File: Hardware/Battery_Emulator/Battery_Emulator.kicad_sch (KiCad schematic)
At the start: 26 parts

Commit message: Added Cell Hierachy
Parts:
- removed C? (x5): C, Capacitor_SMD:C_0805_2012Metric, symbol Device:C
- removed JP? (x2): Jumper_3_Bridged12, symbol Jumper:Jumper_3_Bridged12
- removed PS?: MEE1S1209SC, Converter_DCDC:Converter_DCDC_Murata_MEE1SxxxxSC_THT, symbol Converter_DCDC:MEE1S1209SC
- removed Q?: IRF7343PBF, Package_SO:SOIC-8_3.9x4.9mm_P1.27mm, symbol Transistor_FET:IRF7343PBF
- removed R? (x4): R, Resistor_SMD:R_0805_2012Metric, symbol Device:R
- removed RV? (x2): R_POT, symbol Device:R_POT
- removed U? (x2): 74AHC2G125DP,125, Package_SO:TSSOP-8_3x3mm_P0.65mm, symbol Regulator_Linear:L7805
- removed U?: 74AHC2G125DP,125, Package_SO:TSSOP-8_3x3mm_P0.65mm, symbol Regulator_Linear:LM317L_TO92
- removed U? (x3): 74AHC2G125DP,125, Package_SO:TSSOP-8_3x3mm_P0.65mm, symbol Amplifier_Operational:TL072
- removed U? (x2): 74AHC2G125DP,125, Package_SO:TSSOP-8_3x3mm_P0.65mm, symbol 74xGxx:74AUC2G125
- removed U?: 74AHC2G125DP,125, Package_SO:TSSOP-8_3x3mm_P0.65mm, symbol PR7 Custom:ISO1640BDR
- removed U?: 74AHC2G125DP,125, Package_SO:TSSOP-8_3x3mm_P0.65mm, symbol PR7 Custom:MCP4651T-103E_ST
- added J1: Screw_Terminal_01x02, symbol Connector:Screw_Terminal_01x02
- added U3: 74AHC2G125DP,125, Package_SO:TSSOP-8_3x3mm_P0.65mm, symbol PR7 Custom:74AHC2G125DP,125
- added U5: LM7805_TO220, Package_TO_SOT_THT:TO-220-3_Vertical, symbol Regulator_Linear:LM7805_TO220
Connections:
- net GND: now also J1.2 (Pin_2), U5.2 (GND)
- net +12V: now reaches C?.1
- net +12V: now also J1.1 (Pin_1), U5.1 (VI)
- new net +5V: U5.3 (VO)
- new net SDA_cell_1-7: U3.6
- new net SDA_cell_8-14: U3.3
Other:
- moved on the sheet: C?

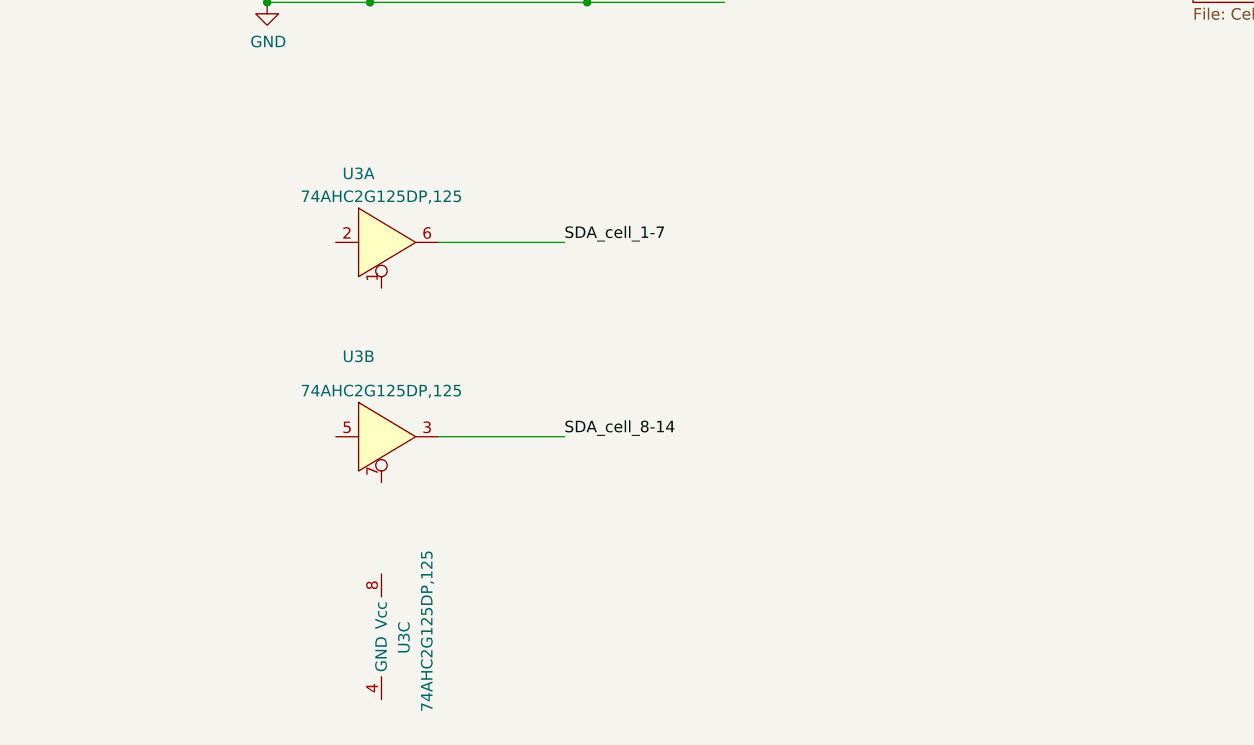
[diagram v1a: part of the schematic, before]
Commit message: Added FT230XS-R
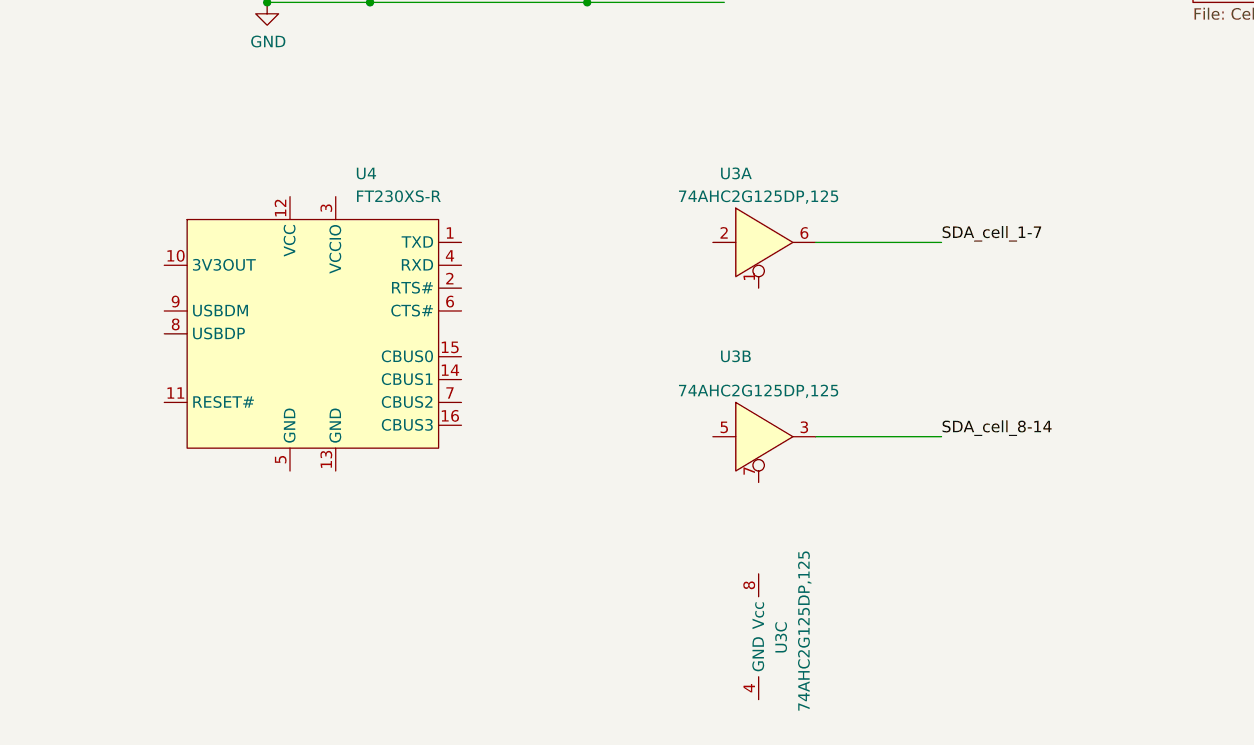
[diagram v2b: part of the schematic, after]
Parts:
- added U4: FT230XS-R, Package_SO:SSOP-16_3.9x4.9mm_P0.635mm, symbol PR7 Custom:FT230XS-R
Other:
- moved on the sheet: U3A, U3B, U3C
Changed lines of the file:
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@@
     (stroke (width 0) (type default))
   )
-  (wire (pts (xy 66.04 101.6) (xy 80.01 101.6))
+  (wire (pts (xy 107.95 101.6) (xy 121.92 101.6))
     (stroke (width 0) (type default))
   )
@@
     (stroke (width 0) (type default))
   )
-  (wire (pts (xy 66.04 80.01) (xy 80.01 80.01))
+  (wire (pts (xy 107.95 80.01) (xy 121.92 80.01))
     (stroke (width 0) (type default))
   )
@@
     (effects (font (size 1.27 1.27)) (justify right bottom))
   )
-  (label "SDA_cell_8-14" (at 80.01 101.6 0) (fields_autoplaced)
+  (label "SDA_cell_8-14" (at 121.92 101.6 0) (fields_autoplaced)
     (effects (font (size 1.27 1.27)) (justify left bottom))
   )
@@
     (effects (font (size 1.27 1.27)) (justify right bottom))
   )
-  (label "SDA_cell_1-7" (at 80.01 80.01 0) (fields_autoplaced)
+  (label "SDA_cell_1-7" (at 121.92 80.01 0) (fields_autoplaced)
     (effects (font (size 1.27 1.27)) (justify left bottom))
   )
@@
     )
   )
-  (symbol (lib_id "PR7 Custom:74AHC2G125DP,125") (at 59.69 80.01 0) (unit 1)
-    (in_bom yes) (on_board yes) (dnp no)
-    (property "Reference" "U3" (at 57.15 72.39 0)
-      (effects (font (size 1.27 1.27)))
-    )
-    (property "Value" "74AHC2G125DP,125" (at 59.69 74.93 0)
-      (effects (font (size 1.27 1.27)))
-    )
-    (property "Footprint" "Package_SO:TSSOP-8_3x3mm_P0.65mm" (at 91.44 77.47 0)
-      (effects (font (size 1.27 1.27)) hide)
-    )
-    (property "Datasheet" "https://www.digikey.nl/en/products/detail/nexperia-usa-inc/74AHC2G125DP-125/1229528" (at 91.44 77.47 0)
+  (symbol (lib_id "PR7 Custom:74AHC2G125DP,125") (at 101.6 80.01 0) (unit 1)
+    (in_bom yes) (on_board yes) (dnp no)
+    (property "Reference" "U3" (at 99.06 72.39 0)
+      (effects (font (size 1.27 1.27)))
+    )
+    (property "Value" "74AHC2G125DP,125" (at 101.6 74.93 0)
+      (effects (font (size 1.27 1.27)))
+    )
+    (property "Footprint" "Package_SO:TSSOP-8_3x3mm_P0.65mm" (at 133.35 77.47 0)
+      (effects (font (size 1.27 1.27)) hide)
+    )
+    (property "Datasheet" "https://www.digikey.nl/en/products/detail/nexperia-usa-inc/74AHC2G125DP-125/1229528" (at 133.35 77.47 0)
       (effects (font (size 1.27 1.27)) hide)
     )
@@
     )
   )
-  (symbol (lib_id "PR7 Custom:74AHC2G125DP,125") (at 59.69 123.19 0) (unit 3)
-    (in_bom yes) (on_board yes) (dnp no)
-    (property "Reference" "U3" (at 62.23 125.73 90)
-      (effects (font (size 1.27 1.27)) (justify left))
-    )
-    (property "Value" "74AHC2G125DP,125" (at 64.77 123.19 90)
-      (effects (font (size 1.27 1.27)))
-    )
-    (property "Footprint" "Package_SO:TSSOP-8_3x3mm_P0.65mm" (at 91.44 120.65 0)
-      (effects (font (size 1.27 1.27)) hide)
-    )
-    (property "Datasheet" "https://www.digikey.nl/en/products/detail/nexperia-usa-inc/74AHC2G125DP-125/1229528" (at 91.44 120.65 0)
+  (symbol (lib_id "PR7 Custom:74AHC2G125DP,125") (at 101.6 123.19 0) (unit 3)
+    (in_bom yes) (on_board yes) (dnp no)
+    (property "Reference" "U3" (at 104.14 125.73 90)
+      (effects (font (size 1.27 1.27)) (justify left))
+    )
+    (property "Value" "74AHC2G125DP,125" (at 106.68 123.19 90)
+      (effects (font (size 1.27 1.27)))
+    )
+    (property "Footprint" "Package_SO:TSSOP-8_3x3mm_P0.65mm" (at 133.35 120.65 0)
+      (effects (font (size 1.27 1.27)) hide)
+    )
+    (property "Datasheet" "https://www.digikey.nl/en/products/detail/nexperia-usa-inc/74AHC2G125DP-125/1229528" (at 133.35 120.65 0)
       (effects (font (size 1.27 1.27)) hide)
     )
@@
     )
   )
-  (symbol (lib_id "PR7 Custom:74AHC2G125DP,125") (at 59.69 101.6 0) (unit 2)
-    (in_bom yes) (on_board yes) (dnp no)
-    (property "Reference" "U3" (at 57.15 92.71 0)
-      (effects (font (size 1.27 1.27)))
-    )
-    (property "Value" "74AHC2G125DP,125" (at 59.69 96.52 0)
-      (effects (font (size 1.27 1.27)))
-    )
-    (property "Footprint" "Package_SO:TSSOP-8_3x3mm_P0.65mm" (at 91.44 99.06 0)
-      (effects (font (size 1.27 1.27)) hide)
-    )
-    (property "Datasheet" "https://www.digikey.nl/en/products/detail/nexperia-usa-inc/74AHC2G125DP-125/1229528" (at 91.44 99.06 0)
-      (effects (font (size 1.27 1.27)) hide)
-    )
+  (symbol (lib_id "PR7 Custom:FT230XS-R") (at 52.07 90.17 0) (unit 1)
+    (in_bom yes) (on_board yes) (dnp no) (fields_autoplaced)
+    (property "Reference" "U4" (at 56.8041 72.39 0)
+      (effects (font (size 1.27 1.27)) (justify left))
+    )
+    (property "Value" "FT230XS-R" (at 56.8041 74.93 0)
+      (effects (font (size 1.27 1.27)) (justify left))
+    )
+    (property "Footprint" "Package_SO:SSOP-16_3.9x4.9mm_P0.635mm" (at 58.42 90.17 0)
+      (effects (font (size 1.27 1.27)) hide)
+    )
+    (property "Datasheet" "https://nl.mouser.com/ProductDetail/FTDI/FT230XS-R?qs=Gp1Yz1mis3XyCLeYOseSng%3D%3D" (at 58.42 90.17 0)
+      (effects (font (size 1.27 1.27)) hide)
+    )
+    (pin "1")
+    (pin "10")
+    (pin "11")
+    (pin "12")
+    (pin "13")
+    (pin "14")
+    (pin "15")
+    (pin "16")
+    (pin "2")
+    (pin "3")
+    (pin "4")
+    (pin "5")
+    (pin "6")
+    (pin "7")
+    (pin "8")
+    (pin "9")
+    (instances
+      (project "Battery_Emulator"
+        (path "/bb7641ff-0dfd-4f4a-b3be-57afbbb9fdac"
+          (reference "U4") (unit 1)
+        )
+      )
+    )
+  )
+  (symbol (lib_id "PR7 Custom:74AHC2G125DP,125") (at 101.6 101.6 0) (unit 2)
+    (in_bom yes) (on_board yes) (dnp no)
+    (property "Reference" "U3" (at 99.06 92.71 0)
+      (effects (font (size 1.27 1.27)))
+    )
+    (property "Value" "74AHC2G125DP,125" (at 101.6 96.52 0)
+      (effects (font (size 1.27 1.27)))
+    )
+    (property "Footprint" "Package_SO:TSSOP-8_3x3mm_P0.65mm" (at 133.35 99.06 0)
+      (effects (font (size 1.27 1.27)) hide)
+    )
+    (property "Datasheet" "https://www.digikey.nl/en/products/detail/nexperia-usa-inc/74AHC2G125DP-125/1229528" (at 133.35 99.06 0)
+      (effects (font (size 1.27 1.27)) hide)
+    )

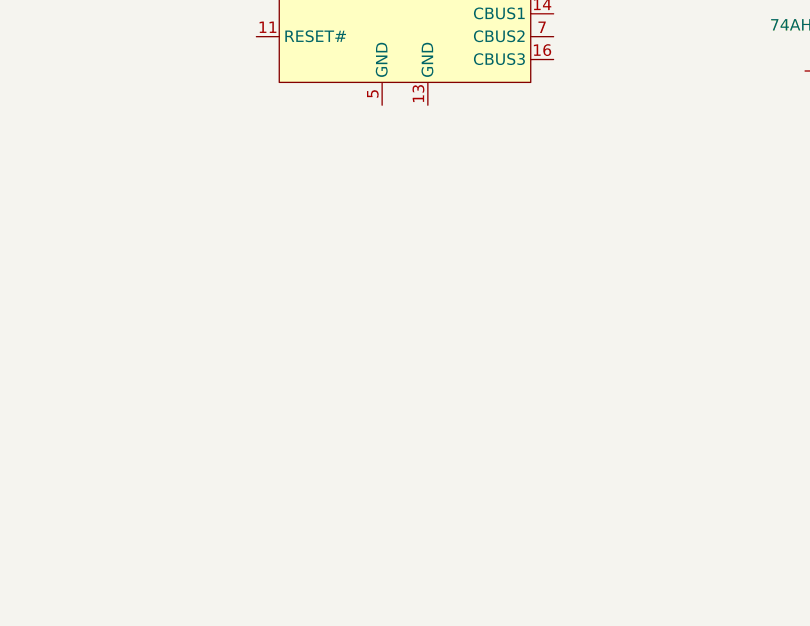
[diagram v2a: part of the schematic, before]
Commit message: Added USB-C and Crystal Components
Symbols + Footprints
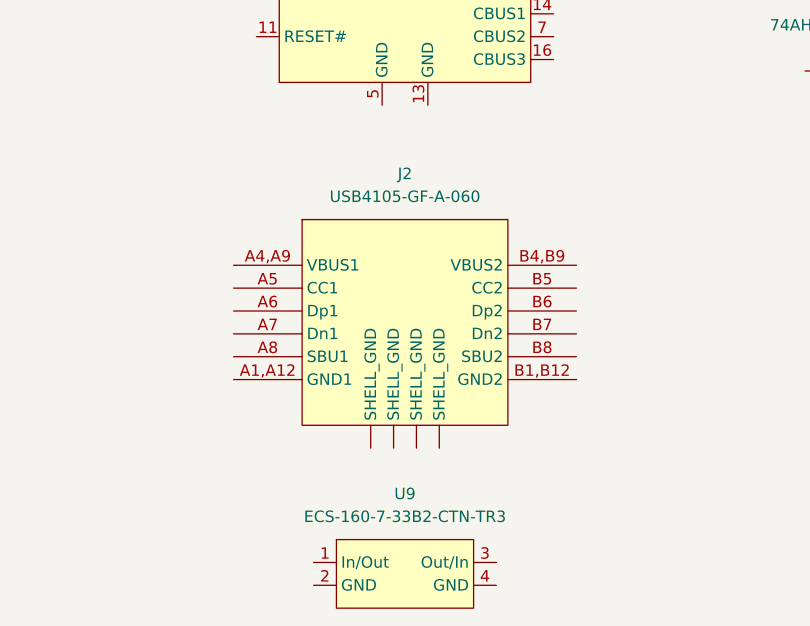
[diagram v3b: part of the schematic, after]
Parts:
- added J2: USB4105-GF-A-060, PR7_Custom_Footprints:GCT_USB4105-GF-A-060, symbol PR7 Custom:USB4105-GF-A-060
- added U9: ECS-160-7-33B2-CTN-TR3, Crystal:Crystal_SMD_3225-4Pin_3.2x2.5mm, symbol PR7 Custom:ECS-160-7-33B2-CTN-TR3
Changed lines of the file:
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@@
+    )
+  )
+  (symbol (lib_id "PR7 Custom:USB4105-GF-A-060") (at 52.07 129.54 0) (unit 1)
+    (in_bom yes) (on_board yes) (dnp no) (fields_autoplaced)
+    (property "Reference" "J2" (at 52.07 113.03 0)
+      (effects (font (size 1.27 1.27)))
+    )
+    (property "Value" "USB4105-GF-A-060" (at 52.07 115.57 0)
+      (effects (font (size 1.27 1.27)))
+    )
+    (property "Footprint" "PR7_Custom_Footprints:GCT_USB4105-GF-A-060" (at 52.07 119.38 0)
+      (effects (font (size 1.27 1.27)) hide)
+    )
+    (property "Datasheet" "https://nl.mouser.com/ProductDetail/GCT/USB4105-GF-A-060?qs=QNEnbhJQKvY2mocwNJzgfA%3D%3D" (at 54.61 154.94 0)
+      (effects (font (size 1.27 1.27)) hide)
+    )
+    (pin "")
+    (pin "")
+    (pin "")
+    (pin "")
+    (pin "A1,A12")
+    (pin "A4,A9")
+    (pin "A5")
+    (pin "A6")
+    (pin "A7")
+    (pin "A8")
+    (pin "B1,B12")
+    (pin "B4,B9")
+    (pin "B5")
+    (pin "B6")
+    (pin "B7")
+    (pin "B8")
+    (instances
+      (project "Battery_Emulator"
+        (path "/bb7641ff-0dfd-4f4a-b3be-57afbbb9fdac"
+          (reference "J2") (unit 1)
+        )
+      )
     )
   )
@@
         )
       )
+    )
+  )
+  (symbol (lib_id "PR7 Custom:ECS-160-7-33B2-CTN-TR3") (at 52.07 157.48 0) (unit 1)
+    (in_bom yes) (on_board yes) (dnp no) (fields_autoplaced)
+    (property "Reference" "U9" (at 52.07 148.59 0)
+      (effects (font (size 1.27 1.27)))
+    )
+    (property "Value" "ECS-160-7-33B2-CTN-TR3" (at 52.07 151.13 0)
+      (effects (font (size 1.27 1.27)))
+    )
+    (property "Footprint" "Crystal:Crystal_SMD_3225-4Pin_3.2x2.5mm" (at 52.07 166.37 0)
+      (effects (font (size 1.27 1.27)) hide)
+    )
+    (property "Datasheet" "https://nl.mouser.com/ProductDetail/ECS/ECS-160-7-33B2-CTN-TR3?qs=1Kr7Jg1SGW%2FBZUGgLr%252BF0g%3D%3D" (at 52.07 163.83 0)
+      (effects (font (size 1.27 1.27)) hide)
+    )
+    (pin "1")
+    (pin "2")
+    (pin "3")
+    (pin "4")
+    (instances
+      (project "Battery_Emulator"
+        (path "/bb7641ff-0dfd-4f4a-b3be-57afbbb9fdac"
+          (reference "U9") (unit 1)
+        )
+      )

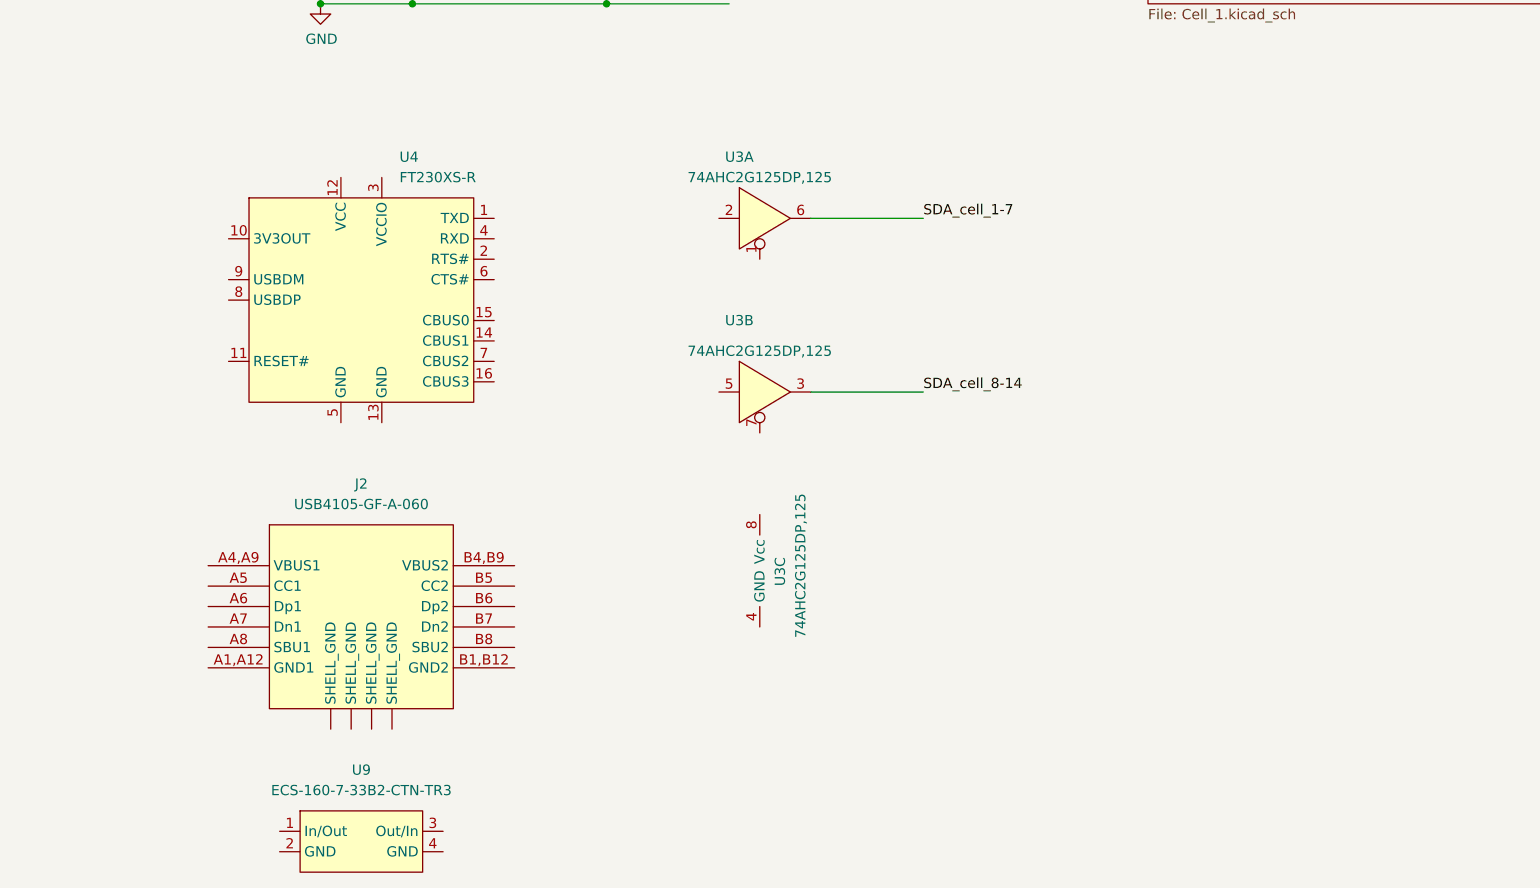
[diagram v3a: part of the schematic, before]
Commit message: Added ATMega and fixed isolated voltage level
12V_ISO -> 9V_ISO
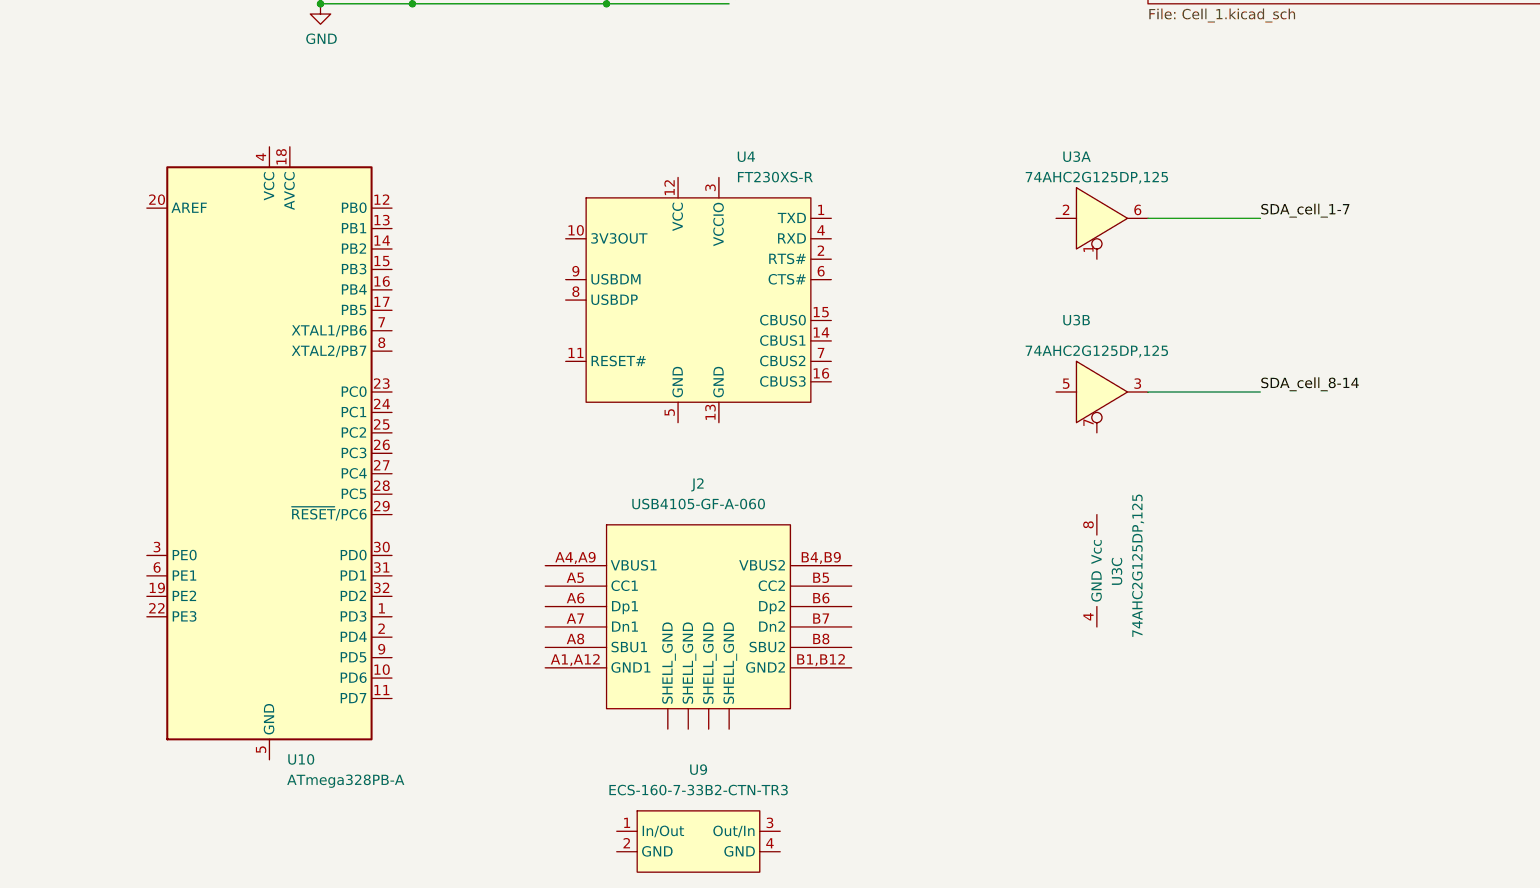
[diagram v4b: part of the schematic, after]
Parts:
- added U10: ATmega328PB-A, Package_QFP:TQFP-32_7x7mm_P0.8mm, symbol MCU_Microchip_ATmega:ATmega328PB-A
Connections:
- new net: U10.21 (GND), U10.5 (GND)
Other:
- moved on the sheet: J2, U3A, U3B, U3C, U4, U9
